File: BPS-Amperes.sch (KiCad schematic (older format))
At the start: 32 parts, among them J1 ShuntConn, J2 LeaderConn, U1 AS8510-ASSM, U2 RO-123.3S_HP, U3 LTC6820, U4 HX1188FNL

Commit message: Updates HX1188 to point to common library
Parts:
- U4: footprint UTSVT_BPS:HXXXX -> UTSVT_Passive:HXXXX; symbol utsvt-bps:HX1188FNL -> utsvt-chips:HX1188FNL
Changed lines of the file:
@@
 $EndComp
 $Comp
-L utsvt-bps:HX1188FNL U4
+L utsvt-chips:HX1188FNL U4
 U 1 1 5F103B51
 P 8550 3800
 F 0 "U4" H 8550 3965 50  0000 C CNN
 F 1 "HX1188FNL" H 8550 3874 50  0000 C CNN
-F 2 "UTSVT_BPS:HXXXX" H 8550 3800 50  0001 C CNN
+F 2 "UTSVT_Passive:HXXXX" H 8550 3800 50  0001 C CNN
 F 3 "" H 8550 3800 50  0001 C CNN
 	1    8550 3800

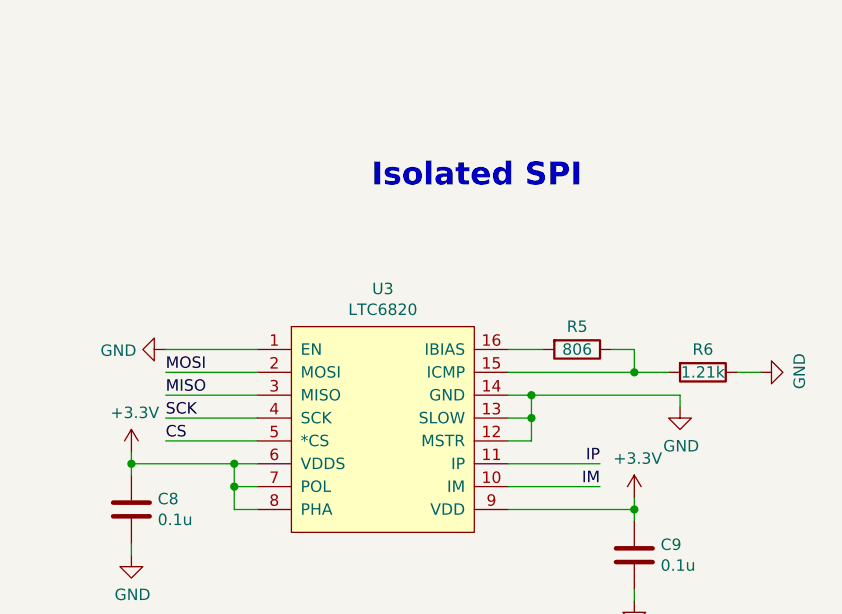
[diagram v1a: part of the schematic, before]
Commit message: Fix timing configuration issue
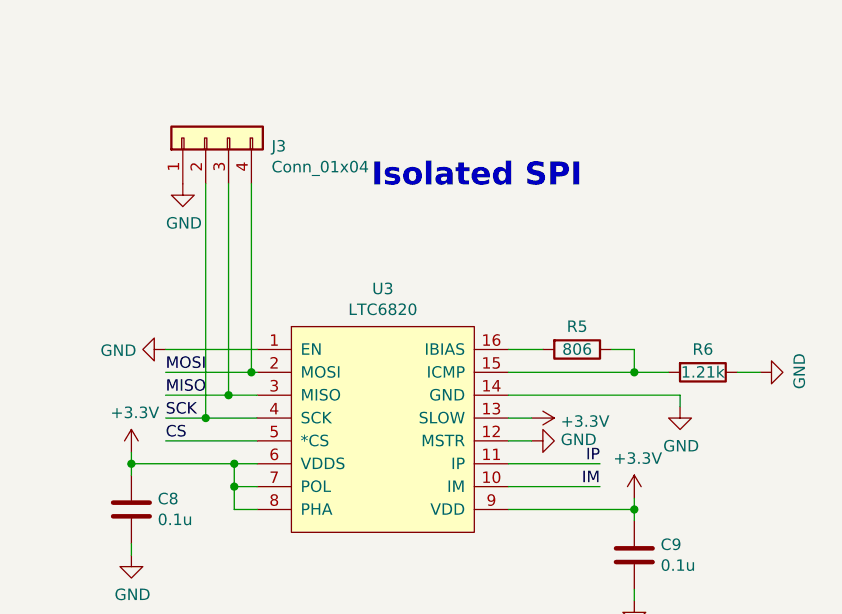
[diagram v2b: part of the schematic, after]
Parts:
- added J3: Conn_01x04, Connector_PinHeader_2.54mm:PinHeader_1x04_P2.54mm_Vertical, symbol Connector_Generic:Conn_01x04
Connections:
- wire segments 112 -> 115
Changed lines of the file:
@@
 	7950 1950 7550 1950
-Wire Wire Line
-	7950 2050 7550 2050
-Wire Wire Line
-	7950 2150 7550 2150
-Wire Wire Line
-	7950 2250 7550 2250
 Wire Wire Line
 	7950 2350 7550 2350
@@
 	10050 2050 10150 2050
 Wire Wire Line
-	9050 2150 9150 2150
-Wire Wire Line
-	9050 2250 9150 2250
-Wire Wire Line
-	9150 2250 9150 2150
-Wire Wire Line
 	9050 2350 9150 2350
-Wire Wire Line
-	9150 2350 9150 2250
-Connection ~ 9150 2250
 Wire Wire Line
 	9050 2450 9450 2450
@@
 	1    0    0    -1
 $EndComp
-Connection ~ 9150 2150
 Text Label 9450 2450 2    50   ~ 0
 IP
@@
 	9800 2200 9800 2150
 Wire Wire Line
-	9150 2150 9800 2150
-Wire Wire Line
 	3850 5100 3900 5100
 Wire Wire Line
@@
 	1    0    0    -1
 $EndComp
+Wire Wire Line
+	9050 2150 9800 2150
+Wire Wire Line
+	9150 2250 9050 2250
+$Comp
+L power:GND #PWR0102
+U 1 1 60A15C7B
+P 9150 2350
+F 0 "#PWR0102" H 9150 2100 50  0001 C CNN
+F 1 "GND" V 9155 2222 50  0000 R CNN
+F 2 "" H 9150 2350 50  0001 C CNN
+F 3 "" H 9150 2350 50  0001 C CNN
+	1    9150 2350
+	0    -1   -1   0
+$EndComp
+$Comp
+L power:+3.3V #PWR0101
+U 1 1 60A29BE4
+P 9150 2250
+F 0 "#PWR0101" H 9150 2100 50  0001 C CNN
+F 1 "+3.3V" V 9165 2378 50  0000 L CNN
+F 2 "" H 9150 2250 50  0001 C CNN
+F 3 "" H 9150 2250 50  0001 C CNN
+	1    9150 2250
+	0    1    1    0
+$EndComp
+$Comp
+L Connector_Generic:Conn_01x04 J3
+U 1 1 60A34776
+P 7725 1025
+F 0 "J3" V 7689 737 50  0000 R CNN
+F 1 "Conn_01x04" V 7598 737 50  0000 R CNN
+F 2 "Connector_PinHeader_2.54mm:PinHeader_1x04_P2.54mm_Vertical" H 7725 1025 50  0001 C CNN
+F 3 "~" H 7725 1025 50  0001 C CNN
+	1    7725 1025
+	0    -1   -1   0
+$EndComp
+$Comp
+L power:GND #PWR0103
+U 1 1 60A357E8
+P 7625 1225
+F 0 "#PWR0103" H 7625 975 50  0001 C CNN
+F 1 "GND" H 7630 1052 50  0000 C CNN
+F 2 "" H 7625 1225 50  0001 C CNN
+F 3 "" H 7625 1225 50  0001 C CNN
+	1    7625 1225
+	1    0    0    -1
+$EndComp
+Wire Wire Line
+	7550 2250 7725 2250
+Wire Wire Line
+	7550 2150 7825 2150
+Wire Wire Line
+	7550 2050 7925 2050
+Wire Wire Line
+	7725 1225 7725 2250
+Connection ~ 7725 2250
+Wire Wire Line
+	7725 2250 7950 2250
+Wire Wire Line
+	7825 1225 7825 2150
+Connection ~ 7825 2150
+Wire Wire Line
+	7825 2150 7950 2150
+Wire Wire Line
+	7925 1225 7925 2050
+Connection ~ 7925 2050
+Wire Wire Line
+	7925 2050 7950 2050
 $EndSCHEMATC
